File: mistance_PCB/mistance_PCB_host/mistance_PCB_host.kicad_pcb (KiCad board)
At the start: 2 copper layers, 86.4 x 99.3 mm, 66 parts, among them J1 USB_B_Micro, J2 USB_B_Micro, J3 GRPB052VWVN-RC, J4 OLED, J5 SMA-J-P-X-ST-TH1, Q1 Q_PMOS_DSG, U1 ESP32-WROOM-32E, U2 TPS61200DRC, U3 MCP73831-2-OT, U4 AMS1117-3.3, U5 CP2104, U6 TPS3839DBZ, U7 SX1278, Y1 Crystal

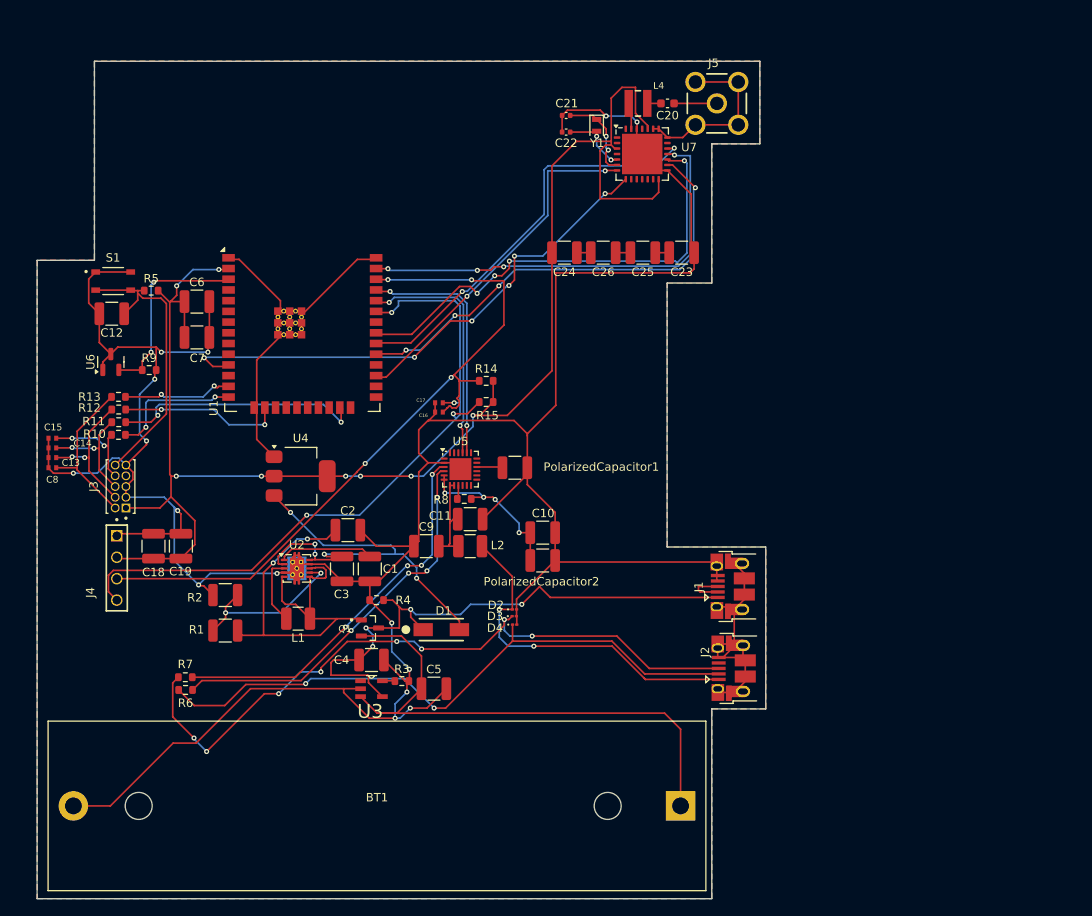
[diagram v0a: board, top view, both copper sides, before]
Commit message: SCH finish PCB writing
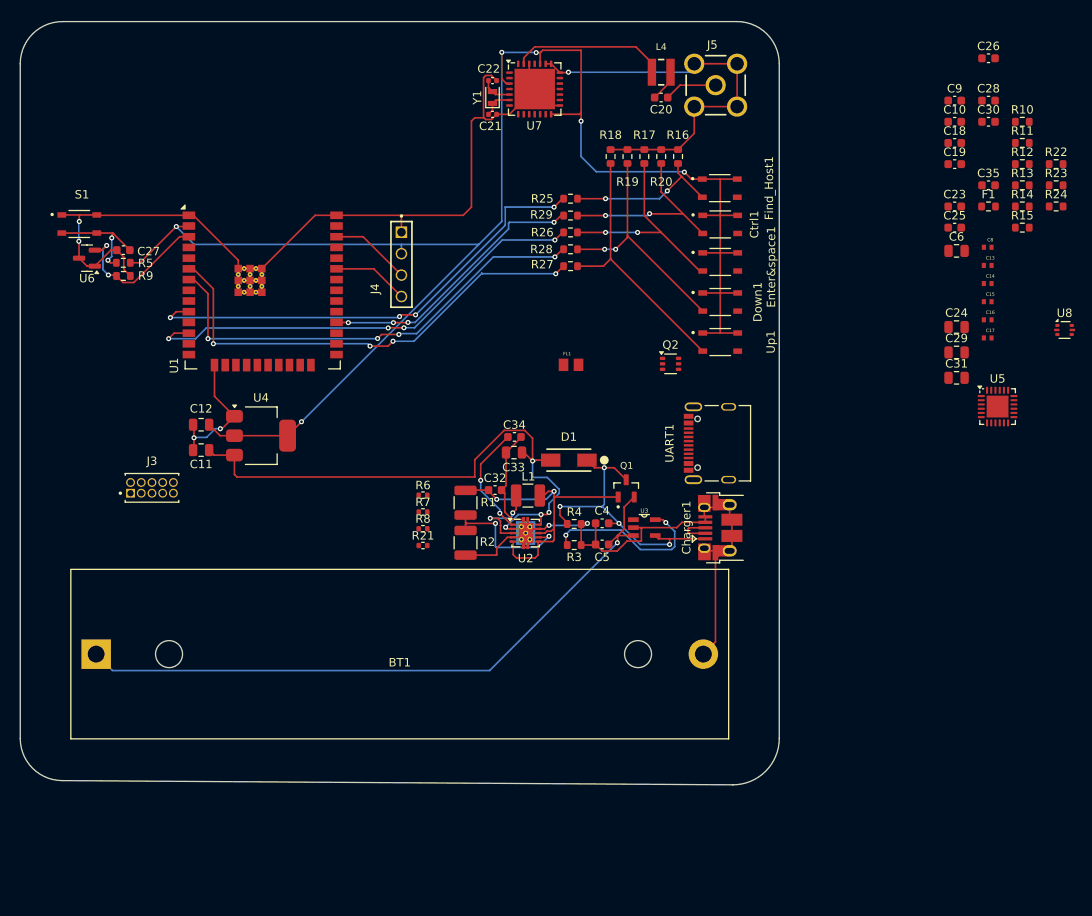
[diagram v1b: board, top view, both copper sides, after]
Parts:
- removed C1, C7: 1uF, Capacitor_SMD:C_1210_3225Metric
- removed C2, PolarizedCapacitor1, PolarizedCapacitor2: 4.7uF, Capacitor_SMD:C_1210_3225Metric
- removed C3: 22uF, Capacitor_SMD:C_1210_3225Metric
- removed D2, D3, D4: PTVS5V0Z1USK, Diode_SMD:D_01005_0402Metric
- removed J1, J2: USB_B_Micro, Connector_USB:USB_Micro-B_Amphenol_10103594-0001LF_Horizontal
- removed L2: 2.2uH, Inductor_SMD:L_1210_3225Metric
- added C27: 0.1uF, Capacitor_SMD:C_0603_1608Metric, F.Cu at (27.2, 42.1)
- added C28: 0.1uF, Capacitor_SMD:C_0603_1608Metric, F.Cu at (129.8, 24.4)
- added C29: 22uF, Capacitor_SMD:C_0805_2012Metric, F.Cu at (126.0, 54.2)
- added C30: 0.1uF, Capacitor_SMD:C_0603_1608Metric, F.Cu at (129.8, 26.9)
- added C31: 22uF, Capacitor_SMD:C_0805_2012Metric, F.Cu at (126.0, 57.2)
- added C32: 4.7uF, Capacitor_SMD:C_0603_1608Metric, F.Cu at (71.3, 70.5)
- added C33: 22uF, Capacitor_SMD:C_0805_2012Metric, F.Cu at (73.5, 66.1)
- added C34: 1uF, Capacitor_SMD:C_0603_1608Metric, F.Cu at (73.6, 64.2)
- added C35: 1uF, Capacitor_SMD:C_0603_1608Metric, F.Cu at (129.8, 34.4)
- added Charger1: Charger, Connector_USB:USB_Micro-B_Amphenol_10103594-0001LF_Horizontal, F.Cu at (98.0, 75.0)
- added Ctrl1: Ctrl, Diode_SMD:SW_SKRPABE010, F.Cu at (98.0, 39.0)
- added Down1: Down, Diode_SMD:SW_SKRPABE010, F.Cu at (98.0, 48.2)
- added Enter&space1: Enter&space, Diode_SMD:SW_SKRPABE010, F.Cu at (98.0, 43.5)
- added F1: Polyfuse, Resistor_SMD:R_0603_1608Metric, F.Cu at (129.8, 36.9)
- added FL1: BLM21PG221SN1D, BLM21PG221SN1D:BEADC2012X105N, F.Cu at (80.3, 55.7)
- added Find_Host1: Find_Host, Diode_SMD:SW_SKRPABE010, F.Cu at (98.0, 34.8)
- added Q2: UMH3N, Package_TO_SOT_SMD:SOT-363_SC-70-6, F.Cu at (92.1, 55.6)
- added R16: 100K, Resistor_SMD:R_0603_1608Metric, F.Cu at (93.0, 31.0)
- added R17: 100K, Resistor_SMD:R_0603_1608Metric, F.Cu at (89.0, 31.0)
- added R18: 100K, Resistor_SMD:R_0603_1608Metric, F.Cu at (85.0, 31.0)
- added R19: 100K, Resistor_SMD:R_0603_1608Metric, F.Cu at (87.0, 31.0)
- added R20: 100K, Resistor_SMD:R_0603_1608Metric, F.Cu at (91.0, 31.0)
- added R21: 22R, Resistor_SMD:R_0402_1005Metric, F.Cu at (62.8, 77.1)
- added R22: 10K, Resistor_SMD:R_0603_1608Metric, F.Cu at (137.8, 31.9)
- added R23: 10K, Resistor_SMD:R_0603_1608Metric, F.Cu at (137.8, 34.4)
- added R24: 10K, Resistor_SMD:R_0603_1608Metric, F.Cu at (137.8, 36.9)
- added R25: 100R, Resistor_SMD:R_0603_1608Metric, F.Cu at (80.2, 36.0)
- added R26: 100R, Resistor_SMD:R_0603_1608Metric, F.Cu at (80.2, 40.0)
- added R27: 100R, Resistor_SMD:R_0603_1608Metric, F.Cu at (80.2, 44.0)
- added R28: 100R, Resistor_SMD:R_0603_1608Metric, F.Cu at (80.2, 42.0)
- added R29: 100R, Resistor_SMD:R_0603_1608Metric, F.Cu at (80.2, 38.0)
- added U8: USBLC6-2P6, Package_TO_SOT_SMD:SOT-666, F.Cu at (138.8, 51.6)
- added UART1: USB_C_Receptacle_USB2.0_16P, 12402012E212A:AMPHENOL_12402012E212A, F.Cu at (99.0, 65.0)
- added Up1: Up, Diode_SMD:SW_SKRPABE010, F.Cu at (98.0, 53.0)
- C10, C9: value 0.1uF -> 4.7uF; footprint Capacitor_SMD:C_1210_3225Metric -> Capacitor_SMD:C_0603_1608Metric
- C11: value 1uF -> 22uF; footprint Capacitor_SMD:C_1210_3225Metric -> Capacitor_SMD:C_0805_2012Metric
- C12: value 0.1uF -> 22uF; footprint Capacitor_SMD:C_1210_3225Metric -> Capacitor_SMD:C_0805_2012Metric
- C18, C19, C23, C25, C26, C4, C5: footprint Capacitor_SMD:C_1210_3225Metric -> Capacitor_SMD:C_0603_1608Metric
- C24, C6: footprint Capacitor_SMD:C_1210_3225Metric -> Capacitor_SMD:C_0805_2012Metric
- R6, R7: value 22 -> 22R; footprint Resistor_SMD:R_0603_1608Metric -> Resistor_SMD:R_0402_1005Metric
- R8: value 4.7K -> 5.1K; footprint Resistor_SMD:R_0603_1608Metric -> Resistor_SMD:R_0402_1005Metric
- moved C8 114.0 mm to (129.7, 41.8), turned to 0 degrees
- moved R10 113.4 mm to (133.8, 26.9), turned to 0 degrees
- moved C13 113.2 mm to (129.7, 43.9), turned to 0 degrees
- moved C14 112.6 mm to (129.7, 46.1), turned to 0 degrees
- moved R11 112.1 mm to (133.8, 29.4), turned to 0 degrees
- moved C15 112.1 mm to (129.7, 48.2), turned to 0 degrees
- moved R12 111.0 mm to (133.8, 31.9), turned to 0 degrees
- moved R13 110.1 mm to (133.8, 34.4), turned to 0 degrees
- moved C18 106.4 mm to (125.8, 29.4), turned to 0 degrees
- moved C19 102.3 mm to (125.8, 31.9), turned to 0 degrees
- moved C6 90.3 mm to (126.0, 42.2)
- moved C9 82.0 mm to (125.8, 24.4)
- moved BT1 71.6 mm to (24.0, 90.0), turned to 0 degrees
- moved C10 69.0 mm to (125.8, 26.9), turned to 0 degrees
- moved R14 66.8 mm to (133.8, 36.9)
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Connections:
- C10 pad 1: GND -> Net-(U5-VPP)
- C10 pad 2: 3.3v OUT CP2104 -> GND
- C11 pad 1: USB 5V OUT -> 5v OUT
- C12 pad 1: GND -> 3.3V OUT
- C12 pad 2: EN -> GND
- C23 pad 1: GND -> Net-(C23-Pad1)
- C23 pad 2: Net-(C23-Pad2) -> GND
- C25 pad 1: Net-(C23-Pad2) -> Net-(C23-Pad1)
- C4 pad 1: Net-(D1-A) -> Net-(Charger1-VBUS)
- C9 pad 1: GND -> Net-(U5-REGIN)
- C9 pad 2: USB 5V OUT -> GND
- Q1 pad 3: Net-(D1-A) -> Net-(Charger1-VBUS)
- R4 pad 1: Net-(D1-A) -> Net-(Charger1-VBUS)
- R6 pad 1: Net-(U5-D-) -> TX
- R6 pad 2: Net-(D4-K) -> Net-(U5-RXD)
- R7 pad 1: Net-(U5-D+) -> RX
- R7 pad 2: Net-(D3-K) -> Net-(U5-TXD)
- R8 pad 1: Net-(U5-~{RST}) -> GND
- R8 pad 2: 3.3v OUT CP2104 -> Net-(UART1-CC2)
- U1 pad 1: Net-(U4-GND) -> GND
- U1 pad 10: unconnected-(U1-IO25-Pad10) -> Find_Host
- U1 pad 12: unconnected-(U1-IO27-Pad12) -> Enter&space
- U1 pad 15: Net-(U4-GND) -> GND
- U1 pad 25: unconnected-(U1-IO0-Pad25) -> IO0
- U1 pad 28: unconnected-(U1-IO17-Pad28) -> Ctrl
- U1 pad 38: Net-(U4-GND) -> GND
- U1 pad 39: Net-(U4-GND) -> GND
- U1 pad 6: unconnected-(U1-IO34-Pad6) -> Up
- U1 pad 7: unconnected-(U1-IO35-Pad7) -> Down
- U3 pad 4: Net-(D1-A) -> Net-(Charger1-VBUS)
- U4 pad 1: Net-(U4-GND) -> GND
- U5 pad 19: unconnected-(U5-~{RTS}-Pad19) -> Net-(U5-~{RTS})
- U5 pad 20: TX -> Net-(U5-RXD)
- U5 pad 21: RX -> Net-(U5-TXD)
- U5 pad 23: unconnected-(U5-~{DTR}-Pad23) -> Net-(U5-~{DTR})
- U5 pad 5: 3.3v OUT CP2104 -> 3.3V OUT
- U5 pad 6: 3.3v OUT CP2104 -> 3.3V OUT
- U5 pad 7: USB 5V OUT -> Net-(U5-REGIN)
- U5 pad 8: USB 5V OUT -> Net-(U5-REGIN)
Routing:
- net GND: track 439.0 -> 242.2 mm, vias 15 -> 7
- net Net-(D3-K): track 83.7 -> 0.00 mm, vias 8 -> 0
- net I2C SCL: track 87.7 -> 9.58 mm, vias 4 -> 0
- net Net-(D4-K): track 74.4 -> 0.00 mm, vias 2 -> 0
- net I2C SDL: track 83.1 -> 9.06 mm, vias 4 -> 0
- net Net-(D1-A): track 69.1 -> 0.00 mm, vias 4 -> 0
- net DIO0(IRQ): track 64.1 -> 0.00 mm, vias 6 -> 0
- net Find_Host: track 0.00 -> 56.2 mm, vias 0 -> 4
- net Up: track 0.00 -> 56.0 mm, vias 0 -> 4
- net MISO: track 55.0 -> 0.00 mm, vias 4 -> 0
- net Down: track 0.00 -> 54.8 mm, vias 0 -> 4
- net Enter&space: track 0.00 -> 54.7 mm, vias 0 -> 4
- net SCK: track 54.5 -> 0.00 mm, vias 4 -> 0
- net MOSI: track 52.6 -> 0.00 mm, vias 4 -> 0
- net NSS(CS): track 48.3 -> 0.00 mm, vias 2 -> 0
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- removed copper zone on B.Cu, net GND
- removed copper zone on F.Cu, net GND
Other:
- board size 86.4 x 99.3 mm -> 90 x 90.5 mm

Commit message: PCB writing
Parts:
- R21: value 22R -> 5.1K
- moved R23 110.8 mm to (29.4, 57.4)
- moved R24 110.6 mm to (29.4, 58.9)
- moved R10 109.3 mm to (27.7, 53.2), turned to 180 degrees
- moved C15 108.7 mm to (21.8, 61.1), turned to -90 degrees
- moved R11 108.4 mm to (27.7, 51.7), turned to 180 degrees
- moved C14 107.8 mm to (22.9, 61.1), turned to -90 degrees
- moved R12 107.7 mm to (27.7, 50.2), turned to 180 degrees
- moved R13 107.1 mm to (27.7, 48.7), turned to 180 degrees
- moved C13 107.0 mm to (24.1, 61.1), turned to -90 degrees
- moved C8 106.3 mm to (25.2, 61.1), turned to -90 degrees
- moved C35 80.7 mm to (53.7, 61.3)
- moved C6 75.2 mm to (53.8, 63.1)
- moved Q2 68.5 mm to (23.6, 57.2)
- moved R22 65.0 mm to (80.8, 63.1), turned to 180 degrees
- moved R15 63.7 mm to (71.0, 50.0)
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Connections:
- UART1 pad A1_B12: (no net) -> GND
- UART1 pad A4_B9: (no net) -> Net-(FL1-Pad2)
- UART1 pad B1_A12: (no net) -> GND
- UART1 pad B4_A9: (no net) -> Net-(FL1-Pad2)
- UART1 pad SH1: (no net) -> GND
- UART1 pad SH2: (no net) -> GND
- UART1 pad SH3: (no net) -> GND
- UART1 pad SH4: (no net) -> GND
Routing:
- net GND: track 242.2 -> 408.7 mm, vias 7 -> 20
- net 3.3V OUT: track 198.5 -> 279.0 mm, vias 6 -> 13
- net DIO0(IRQ): track 0.00 -> 66.7 mm, vias 0 -> 6
- net Net-(U5-~{RTS}): track 0.00 -> 58.8 mm, vias 0 -> 4
- net Net-(U5-~{DTR}): track 0.00 -> 55.1 mm, vias 0 -> 2
- net NSS(CS): track 0.00 -> 46.7 mm, vias 0 -> 8
- net MISO: track 0.00 -> 45.3 mm, vias 0 -> 8
- net RESET: track 0.00 -> 45.3 mm, vias 0 -> 8
- net SCK: track 0.00 -> 41.7 mm, vias 0 -> 8
- net MOSI: track 0.00 -> 39.2 mm, vias 0 -> 4
- net TX: track 0.00 -> 37.4 mm, vias 0 -> 4
- net RX: track 0.00 -> 36.7 mm, vias 0 -> 4
- net IO0: track 0.00 -> 32.4 mm, vias 0 -> 2
- net MTDO: track 0.00 -> 24.7 mm, vias 0 -> 4
- net Net-(FL1-Pad2): track 0.00 -> 23.0 mm, vias 0 -> 3
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- added copper zone on B.Cu, net GND
- added copper zone on F.Cu, net GND

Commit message: host PCB and SCH finish
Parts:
- moved C22 1.40 mm to (71.0, 20.6)
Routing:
- net GND: track 408.7 -> 416.6 mm
- net 3.3V OUT: track 279.0 -> 284.3 mm, vias 13 -> 18
- net Net-(U1-EN): track 20.2 -> 23.2 mm
- net Net-(Ctrl1-Pad3): track 29.2 -> 27.1 mm, vias 4 -> 2
- net Net-(Enter&space1-Pad3): track 32.0 -> 29.9 mm, vias 4 -> 2
- net Net-(Down1-Pad3): track 34.1 -> 32.1 mm, vias 4 -> 2
- net Net-(Find_Host1-Pad3): track 24.4 -> 22.8 mm, vias 4 -> 2
- net Net-(UART1-CC1): track 4.66 -> 6.12 mm
- net Net-(U7-XTA): track 3.66 -> 5.06 mm
- net I2C SCL: track 23.5 -> 24.4 mm

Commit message: host PCB and SCH bug fix
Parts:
- removed C25: 1uF, Capacitor_SMD:C_0603_1608Metric
- removed C26: 10uF, Capacitor_SMD:C_0603_1608Metric
- removed R5: 10K, Resistor_SMD:R_0603_1608Metric
- removed U6: TPS3839DBZ, Package_TO_SOT_SMD:SOT-23
- added C37: 1uF, Capacitor_SMD:C_0603_1608Metric, F.Cu at (30.3, 39.8)
- added R30: 22R, Resistor_SMD:R_0402_1005Metric, F.Cu at (27.4, 39.7)
- R9: value 100K -> 10K
- moved R9 18.3 mm to (32.5, 62.7)
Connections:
- C23 pad 1: Net-(C23-Pad1) -> 3.3V OUT
- C24 pad 1: Net-(C24-Pad1) -> GND
- C27 pad 2: EN -> Net-(C27-Pad2)
- D1 pad A: 5v OUT -> (no net)
- D1 pad C: Net-(Charger1-VBUS) -> (no net)
- R9 pad 1: Net-(U1-EN) -> EN
- R9 pad 2: GND -> 3.3V OUT
- S1 pad 3: EN -> Net-(C27-Pad2)
- S1 pad 4: EN -> Net-(C27-Pad2)
- U1 pad 3: Net-(U1-EN) -> EN
- UART1 pad A1_B12: GND -> (no net)
- UART1 pad A4_B9: Net-(FL1-Pad2) -> (no net)
- UART1 pad B1_A12: GND -> (no net)
- UART1 pad B4_A9: Net-(FL1-Pad2) -> (no net)
- UART1 pad SH1: GND -> (no net)
- UART1 pad SH2: GND -> (no net)
- UART1 pad SH3: GND -> (no net)
- UART1 pad SH4: GND -> (no net)
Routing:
- net Net-(U1-EN): track 23.2 -> 0.00 mm, vias 4 -> 0
- net Net-(FL1-Pad2): track 23.0 -> 0.00 mm, vias 3 -> 0
- net EN: track 31.6 -> 52.5 mm, vias 2 -> 3
- net GND: track 416.6 -> 405.9 mm
- net Net-(C27-Pad2): track 0.00 -> 9.98 mm
- net Net-(Charger1-VBUS): track 36.3 -> 33.9 mm
- net 5v OUT: track 68.2 -> 66.0 mm
- net 3.3V OUT: track 284.3 -> 286.0 mm
- net Net-(C25-Pad2): track 1.67 -> 0.00 mm
- net Net-(C24-Pad1): track 1.55 -> 0.00 mm
- net Net-(C23-Pad1): track 1.45 -> 0.00 mm
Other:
- outline, holes or cut-outs redrawn

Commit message: host code
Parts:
- R16, R17, R18, R19, R20: value 100K -> 10K
- moved R18 0.89 mm to (85.0, 30.1)
- moved R19 0.87 mm to (87.0, 30.1)
- moved R17 0.87 mm to (89.0, 30.1)
- moved R20 0.87 mm to (91.0, 30.1)
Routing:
- net Net-(R18-Pad1): track 35.2 -> 36.1 mm
- net Net-(Down1-Pad3): track 32.1 -> 32.9 mm
- net Net-(Enter&space1-Pad3): track 29.9 -> 30.8 mm
- net Net-(Ctrl1-Pad3): track 27.4 -> 28.3 mm
- net GND: track 405.9 -> 406.6 mm

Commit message: host code modify & host PCB and SCH modify
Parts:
- added C25: 22uF, Capacitor_SMD:C_0805_2012Metric, F.Cu at (39.0, 76.4)
- added C7: 1uF, Capacitor_SMD:C_0603_1608Metric, F.Cu at (38.9, 74.5)
- added R31: 1K, Resistor_SMD:R_0603_1608Metric, F.Cu at (64.4, 66.8)
- added R5: 100R, Resistor_SMD:R_0402_1005Metric, F.Cu at (64.2, 68.1)
- added U6: L86-M33, L86-M33:XCVR_L86-M33, F.Cu at (51.9, 73.1)
- moved C35 38.9 mm to (20.0, 42.0)
- moved C6 38.9 mm to (20.0, 43.8)
- moved R9 19.0 mm to (18.9, 76.0)
- moved U4 19.0 mm to (30.0, 77.4)
- moved C11 19.0 mm to (22.9, 79.1)
- moved C12 19.0 mm to (22.9, 76.1)
- moved BT1 4.00 mm to (24.0, 94.0)
- moved S1 2.00 mm to (20.0, 39.0)
- moved Up1 2.00 mm to (98.0, 55.0)
- moved Down1 1.25 mm to (98.0, 49.5)
- moved Find_Host1 0.75 mm to (98.0, 34.0)
- moved Enter&space1 0.58 mm to (97.9, 44.1)
- moved Ctrl1 0.06 mm to (97.9, 39.1)
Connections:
- U1 pad 26: unconnected-(U1-IO4-Pad26) -> GPS_Reset
- U1 pad 8: unconnected-(U1-IO32-Pad8) -> GPS_TX
- U1 pad 9: unconnected-(U1-IO33-Pad9) -> GPS_Rx
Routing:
- net GND: track 406.6 -> 478.4 mm, vias 20 -> 21
- net GPS_TX: track 0.00 -> 38.1 mm, vias 0 -> 2
- net 3.3V OUT: track 286.0 -> 321.9 mm, vias 18 -> 20
- net GPS_Rx: track 0.00 -> 34.3 mm, vias 0 -> 2
- net 5v OUT: track 66.0 -> 91.5 mm, vias 4 -> 6
- net GPS_Reset: track 0.00 -> 20.5 mm, vias 0 -> 4
- net EN: track 52.5 -> 61.2 mm
- net Net-(U6-~{RESET}): track 0.00 -> 8.21 mm
- net Net-(R18-Pad1): track 36.1 -> 38.5 mm
- net Net-(BT1-+): track 78.5 -> 80.7 mm
- net Net-(C27-Pad2): track 9.98 -> 12.0 mm
- net Net-(Down1-Pad3): track 32.9 -> 34.2 mm
- net Net-(Ctrl1-Pad3): track 28.3 -> 27.4 mm

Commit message: PCB and code modify
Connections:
- FL1 pad 2: Net-(FL1-Pad2) -> 5v OUT
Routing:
- net 5v OUT: track 91.5 -> 111.4 mm, vias 6 -> 8
